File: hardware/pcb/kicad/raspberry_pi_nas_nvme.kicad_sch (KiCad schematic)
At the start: 44 parts, among them J1 2024100002, J2 AUX5V INPUT — CONNECTOR TBD, J3 1-2199230-6, U1 JMS583-QHFA0A, U2 TPD4E05U06DQAR, U3 TPD4E05U06DQAR, U4 TPD4E05U06DQAR, U5 POWER_PATH_TBD, U6 W25Q16JVSNIQ TR, U7 TPS54302DDCR, Y1 ABM8-25.000MHZ-B2-T

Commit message: Correct JMS583 power, reset, crystal, LED, and split-supply design
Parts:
- removed U5: POWER_PATH_TBD, symbol RaspberryPiNAS_Parts:PowerPath_Placeholder
- added C24, C25: 30pF C0G 5%, Capacitor_SMD:C_0603_1608Metric_Pad1.08x0.95mm_HandSolder, symbol Device:C
- added C26: 1uF X7R 10%, Capacitor_SMD:C_0603_1608Metric_Pad1.08x0.95mm_HandSolder, symbol Device:C
- added R10, R9: 100k 1%, Resistor_SMD:R_0603_1608Metric_Pad0.98x0.95mm_HandSolder, symbol Device:R
- added R8: 510k, Resistor_SMD:R_0603_1608Metric_Pad0.98x0.95mm_HandSolder, symbol Device:R
- R2: value 10k VERIFY -> 330k 1%
- R3: value 1k VERIFY -> 1k
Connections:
- net ACT_LED_N: now also U1.8 (GPIO4); no longer U1.57 (GPIO12)
- net AUX5V: now also C15.1, C16.1, C17.1, U7.3 (VIN), U7.5 (EN)
- net GND: now also C24.2, C25.2, C26.2, R10.2
- net JMS_RST_N: now also C26.1
- net USB5V: now also U1.1 (VDDREG), R9.1
- net XTAL_IN: now also C24.1, R8.1
- net XTAL_OUT: now also C25.1, R8.2
- net USB_VBUS_SENSE: now reaches U1.10 (GPIO6)
- net USB_VBUS_SENSE: now also R10.1, R9.2
- net 1V2_JMS renamed 1V0_JMS
- removed net 5V_SYS: C15.1, C16.1, C17.1, U1.1 (VDDREG), U7.3 (VIN), U7.5 (EN)
- no-connect marks 37 -> 36
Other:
- note added: "1V0 core/analog rail; EP and TME grounded; 330k/1uF reset; GPIO4 active-low LED; calculated 30pF crystal loads."
- note added: "AUX5V and 3V3_NVME must be valid before USB enumeration when SSD access is required."
- note added: "JMS583 CORRECTIVE REVIEW APPLIED — SEE schematic_review.md"
- note added: "SPLIT POWER: USB5V -> JMS583; AUX5V -> NVMe 3V3 buck; COMMON GND"
- note added: "TPS54302 is limited to 3 A maximum; verify SSD peak/transient demand before release."
- note removed: "Inductor/capacitor voltage, ripple-current, DC-bias and thermal ratings require final MPN selection."
- note removed: "JMS583 public pin table used. Confirm EP grounding, reset pull-up, crystal load network, internal-regulator rail topology and LED polarity."
- note removed: "POWER-PATH PLACEHOLDER — NO USB5V/AUX5V SHORT IS PRESENT"
- note removed: "Select a reverse-current-blocking 5 V power mux / ideal-diode solution and rated AUX connector before PCB release."
- note removed: "VERIFY AGAINST JMS583 REFERENCE DESIGN BEFORE PCB RELEASE"

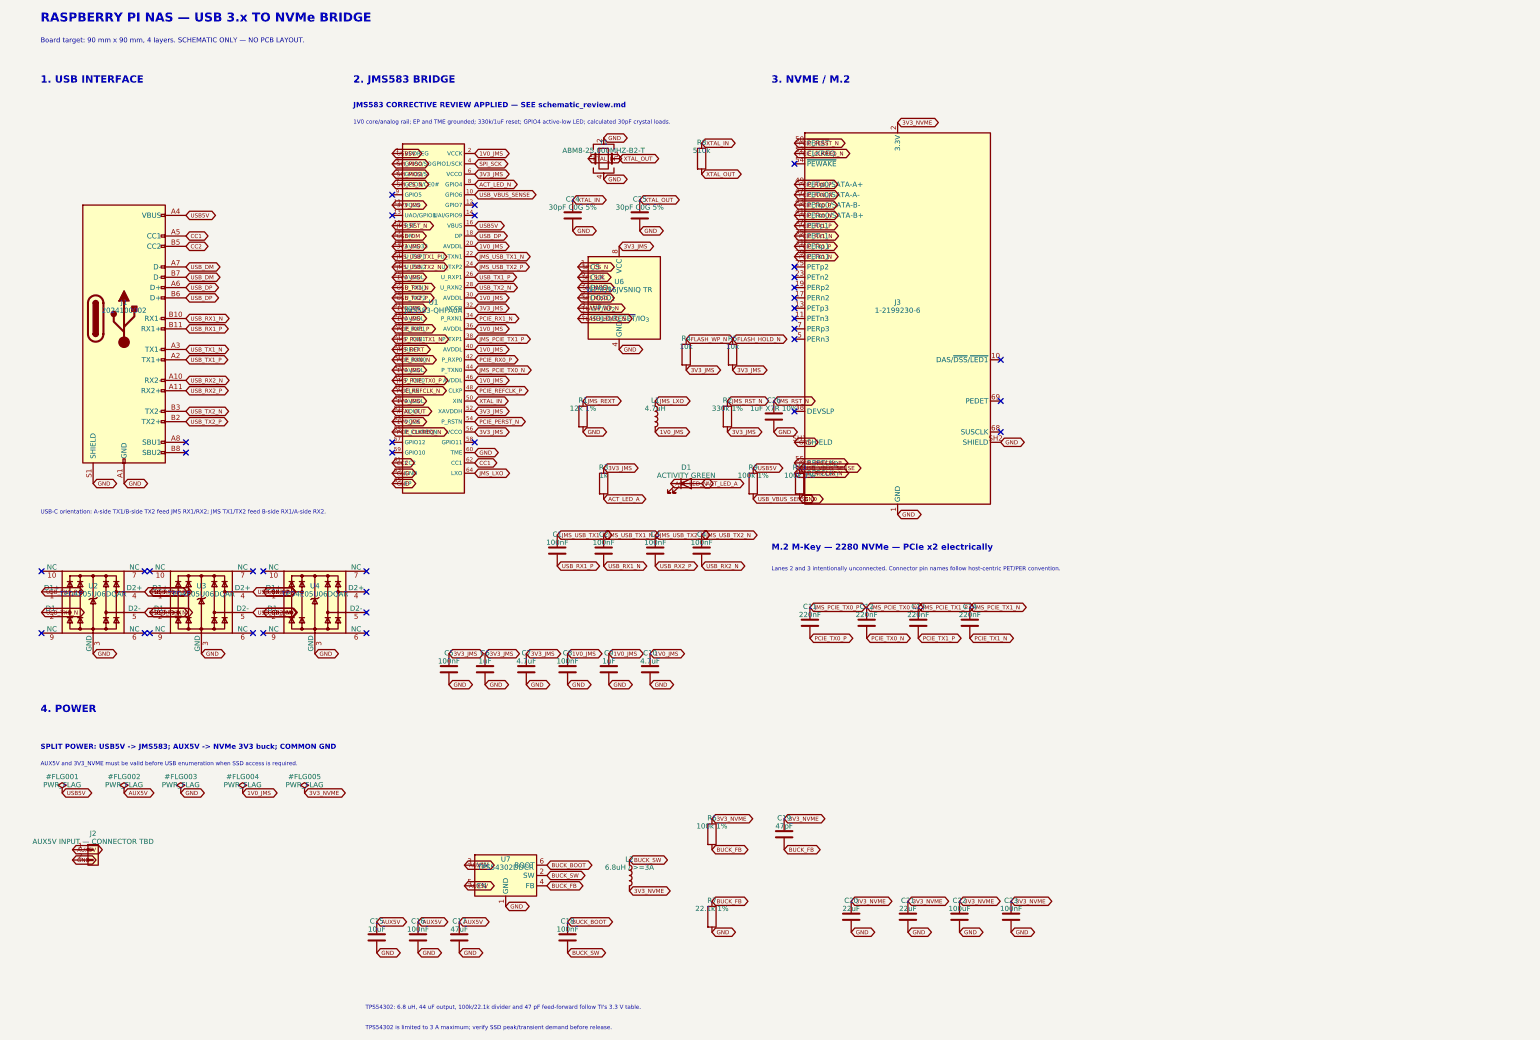
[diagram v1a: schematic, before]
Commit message: Clean up KiCad schematic presentation
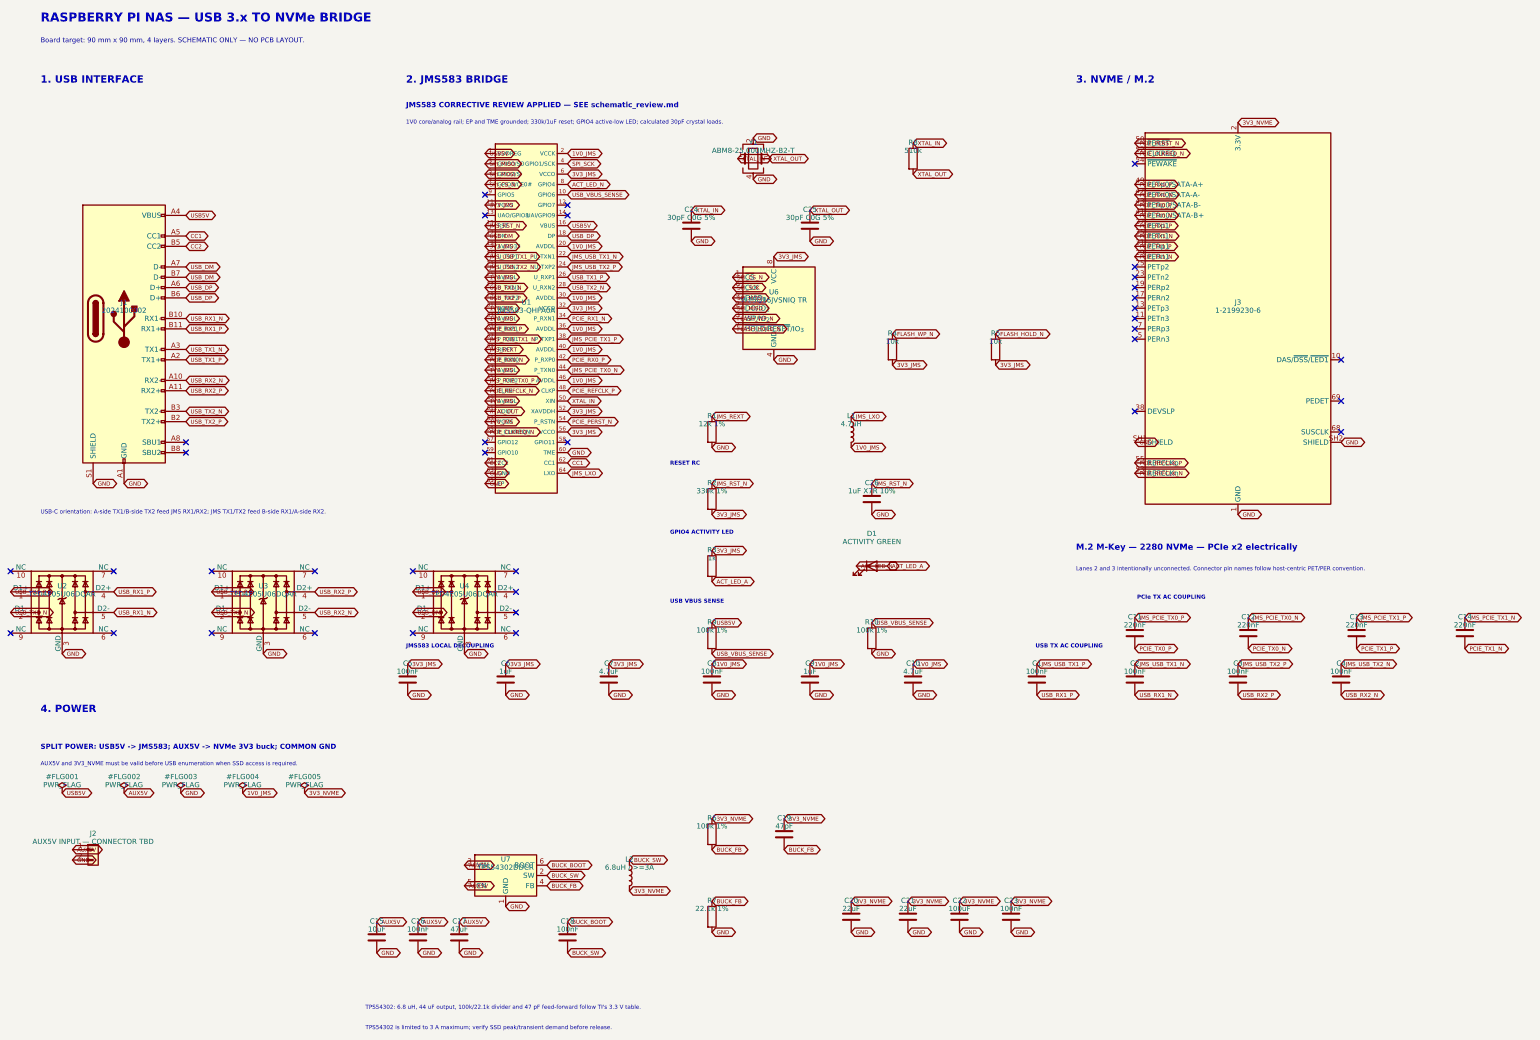
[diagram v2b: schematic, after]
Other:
- note added: "GPIO4 ACTIVITY LED"
- note added: "JMS583 LOCAL DECOUPLING"
- note added: "PCIe TX AC COUPLING"
- note added: "RESET RC"
- note added: "USB TX AC COUPLING"
- note added: "USB VBUS SENSE"
